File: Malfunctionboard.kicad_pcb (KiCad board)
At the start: 2 copper layers, 141.4 x 32.7 mm, 270 parts, among them J101 Conn_02x05_Odd_Even, J102 Conn_02x05_Odd_Even, J201 Conn_Coaxial, J202 Conn_Coaxial, J301 Conn_Coaxial, J302 Conn_Coaxial, J401 Conn_Coaxial, J402 Conn_Coaxial, J501 Conn_Coaxial, J502 Conn_Coaxial, J601 Conn_Coaxial, J602 Conn_Coaxial, J701 Conn_Coaxial, J702 Conn_Coaxial, J801 Conn_Coaxial, J802 Conn_Coaxial, J901 Conn_Coaxial, J902 Conn_Coaxial, Q101 NTR5103NT1G, Q102 RSC002P03T316, Q103 RSC002P03T316, Q104 NTR5103NT1G, Q201 NTR5103NT1G, Q202 NTR5103NT1G, Q301 NTR5103NT1G, Q302 NTR5103NT1G, Q401 NTR5103NT1G, Q402 NTR5103NT1G, Q501 NTR5103NT1G, Q502 NTR5103NT1G, Q601 NTR5103NT1G, Q602 NTR5103NT1G, Q701 NTR5103NT1G, Q702 NTR5103NT1G, Q801 NTR5103NT1G, Q802 NTR5103NT1G, Q901 NTR5103NT1G, Q902 NTR5103NT1G, U201 LM339PW, U301 LM339PW, U401 LM339PW, U501 LM339PW, U601 LM339PW, U701 LM339PW, U801 LM339PW, U901 LM339PW

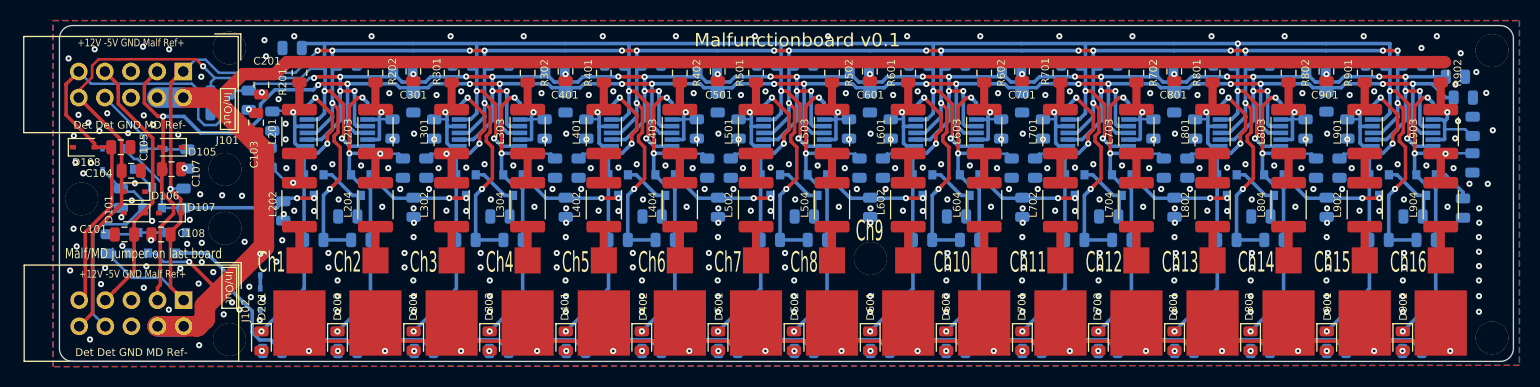
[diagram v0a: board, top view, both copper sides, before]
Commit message: Added: Through holes in the coaxial pads, for use as interfacebox module; README, LICENSE.
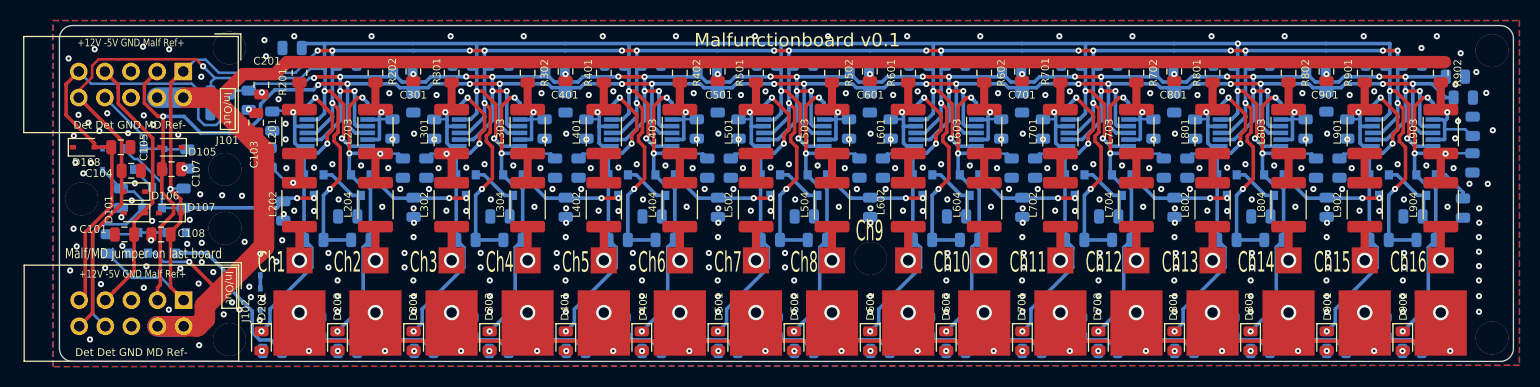
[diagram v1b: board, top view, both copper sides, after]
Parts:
- moved SYM101 3.86 mm to (110.2, 126.2)
- moved C812 1.02 mm to (183.3, 130.3)
- moved C212 1.02 mm to (94.5, 130.3)
- moved C312 1.02 mm to (109.3, 130.3)
- moved C412 1.02 mm to (124.1, 130.3)
- moved C512 1.02 mm to (138.9, 130.3)
- moved C612 1.02 mm to (153.7, 130.3)
- moved C712 1.02 mm to (168.5, 130.3)
- moved C912 1.02 mm to (198.1, 130.3)
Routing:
- net Net-(D701-Pad1): track 29.0 -> 29.6 mm
- net Net-(D501-Pad1): track 29.0 -> 29.6 mm
- net Net-(D801-Pad1): track 29.0 -> 29.6 mm
- net Net-(D301-Pad1): track 29.0 -> 29.6 mm
- net Net-(D601-Pad1): track 29.0 -> 29.6 mm
- net Net-(D901-Pad1): track 29.0 -> 29.6 mm
- net Net-(D401-Pad1): track 29.0 -> 29.6 mm
- net Net-(D201-Pad1): track 29.0 -> 29.5 mm
- net Net-(J902-Pad1): vias 0 -> 1
- net Net-(J901-Pad1): vias 0 -> 1
- net Net-(J802-Pad1): vias 0 -> 1
- net Net-(J801-Pad1): vias 0 -> 1
- net Net-(J702-Pad1): vias 0 -> 1
- net Net-(J701-Pad1): vias 0 -> 1
- net Net-(J602-Pad1): vias 0 -> 1
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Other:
- board text added: "(8ch:R101)"
- board text added: "02/2020 v0.1"
- board text removed: "11/2019 v0.1"

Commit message: Fixed: wrong pin layout for comparator
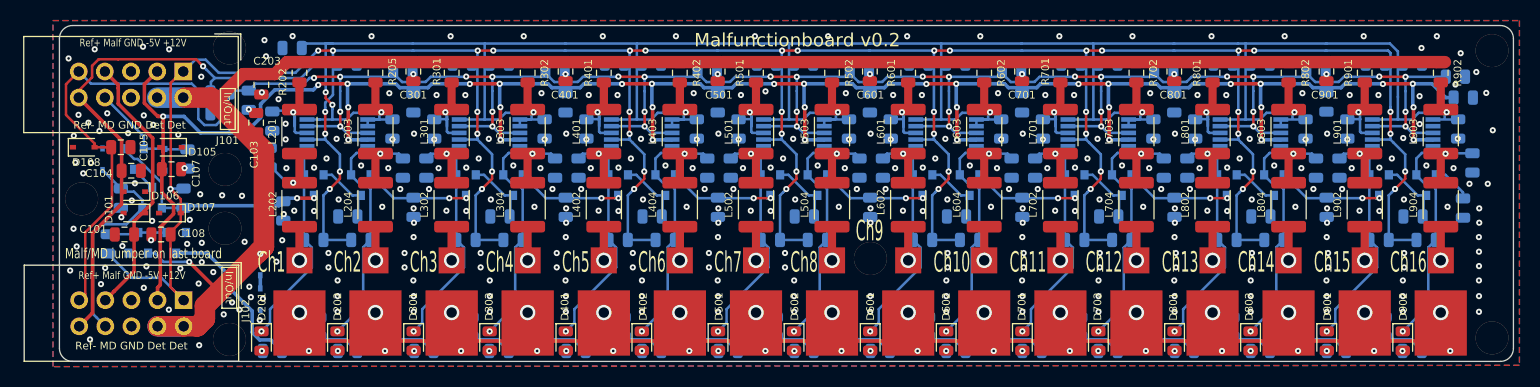
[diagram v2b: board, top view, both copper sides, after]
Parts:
- moved C904 1.44 mm to (205.2, 111.0), turned to 90 degrees
- renumbered C208 to C201, C209 to C202, C201 to C203, C210 to C204, C202 to C205, C203 to C206, C211 to C207, C206 to C208, C204 to C209, C207 to C210, C205 to C211, C309 to C307, C307 to C309, C409 to C407, C407 to C409, C509 to C507, C507 to C509, C609 to C607, C607 to C609, C709 to C707, C707 to C709, C809 to C807, C807 to C809, C909 to C907, C907 to C909, R203 to R201, R201 to R202, R204 to R203, R205 to R204, R202 to R205
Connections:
- C205 pad 2: Net-(C202-Pad2) -> Net-(C205-Pad2)
- C209 pad 2: Net-(C204-Pad2) -> Net-(C209-Pad2)
- C307 pad 2: +12V -> /Ref-
- C309 pad 2: /Ref- -> +12V
- C407 pad 2: +12V -> /Ref-
- C409 pad 2: /Ref- -> +12V
- C507 pad 2: +12V -> /Ref-
- C509 pad 2: /Ref- -> +12V
- C607 pad 2: +12V -> /Ref-
- C609 pad 2: /Ref- -> +12V
- C707 pad 2: +12V -> /Ref-
- C709 pad 2: /Ref- -> +12V
- C807 pad 2: +12V -> /Ref-
- C809 pad 2: /Ref- -> +12V
- C907 pad 2: +12V -> /Ref-
- C909 pad 2: /Ref- -> +12V
- L201 pad 2: Net-(C202-Pad2) -> Net-(C205-Pad2)
- L203 pad 2: Net-(C204-Pad2) -> Net-(C209-Pad2)
- R202 pad 2: Net-(C202-Pad2) -> Net-(C205-Pad2)
- R205 pad 2: Net-(C204-Pad2) -> Net-(C209-Pad2)
- U201 pad 10: /Ref+ -> Net-(C209-Pad2)
- U201 pad 11: -5V -> /Ref+
- U201 pad 12: Net-(C204-Pad2) -> -5V
- U201 pad 13: /Ref- -> Net-(D202-Pad1)
- U201 pad 2: Net-(C202-Pad2) -> Net-(D201-Pad1)
- U201 pad 3: /Ref+ -> +12V
- U201 pad 4: +12V -> Net-(C205-Pad2)
- U201 pad 5: Net-(C202-Pad2) -> /Ref+
- U201 pad 7: Net-(D201-Pad1) -> Net-(C205-Pad2)
- U201 pad 8: Net-(D202-Pad1) -> /Ref-
- U201 pad 9: Net-(C204-Pad2) -> Net-(C209-Pad2)
- U301 pad 10: /Ref+ -> Net-(C304-Pad2)
- U301 pad 11: -5V -> /Ref+
- U301 pad 12: Net-(C304-Pad2) -> -5V
- U301 pad 13: /Ref- -> Net-(D302-Pad1)
- U301 pad 2: Net-(C302-Pad2) -> Net-(D301-Pad1)
- U301 pad 3: /Ref+ -> +12V
- U301 pad 4: +12V -> Net-(C302-Pad2)
- U301 pad 5: Net-(C302-Pad2) -> /Ref+
- U301 pad 7: Net-(D301-Pad1) -> Net-(C302-Pad2)
- U301 pad 8: Net-(D302-Pad1) -> /Ref-
- U401 pad 10: /Ref+ -> Net-(C404-Pad2)
- U401 pad 11: -5V -> /Ref+
- U401 pad 12: Net-(C404-Pad2) -> -5V
- U401 pad 13: /Ref- -> Net-(D402-Pad1)
- U401 pad 2: Net-(C402-Pad2) -> Net-(D401-Pad1)
- U401 pad 3: /Ref+ -> +12V
- U401 pad 4: +12V -> Net-(C402-Pad2)
- U401 pad 5: Net-(C402-Pad2) -> /Ref+
- U401 pad 7: Net-(D401-Pad1) -> Net-(C402-Pad2)
- U401 pad 8: Net-(D402-Pad1) -> /Ref-
- U501 pad 10: /Ref+ -> Net-(C504-Pad2)
- U501 pad 11: -5V -> /Ref+
- U501 pad 12: Net-(C504-Pad2) -> -5V
- U501 pad 13: /Ref- -> Net-(D502-Pad1)
- U501 pad 2: Net-(C502-Pad2) -> Net-(D501-Pad1)
- U501 pad 3: /Ref+ -> +12V
- U501 pad 4: +12V -> Net-(C502-Pad2)
- U501 pad 5: Net-(C502-Pad2) -> /Ref+
- U501 pad 7: Net-(D501-Pad1) -> Net-(C502-Pad2)
- U501 pad 8: Net-(D502-Pad1) -> /Ref-
- U601 pad 10: /Ref+ -> Net-(C604-Pad2)
- U601 pad 11: -5V -> /Ref+
- U601 pad 12: Net-(C604-Pad2) -> -5V
- U601 pad 13: /Ref- -> Net-(D602-Pad1)
- U601 pad 2: Net-(C602-Pad2) -> Net-(D601-Pad1)
- U601 pad 3: /Ref+ -> +12V
- U601 pad 4: +12V -> Net-(C602-Pad2)
- U601 pad 5: Net-(C602-Pad2) -> /Ref+
- U601 pad 7: Net-(D601-Pad1) -> Net-(C602-Pad2)
- U601 pad 8: Net-(D602-Pad1) -> /Ref-
- U701 pad 10: /Ref+ -> Net-(C704-Pad2)
- U701 pad 11: -5V -> /Ref+
- U701 pad 12: Net-(C704-Pad2) -> -5V
- U701 pad 13: /Ref- -> Net-(D702-Pad1)
- U701 pad 2: Net-(C702-Pad2) -> Net-(D701-Pad1)
- U701 pad 3: /Ref+ -> +12V
- U701 pad 4: +12V -> Net-(C702-Pad2)
- U701 pad 5: Net-(C702-Pad2) -> /Ref+
- U701 pad 7: Net-(D701-Pad1) -> Net-(C702-Pad2)
- U701 pad 8: Net-(D702-Pad1) -> /Ref-
- U801 pad 10: /Ref+ -> Net-(C804-Pad2)
- U801 pad 11: -5V -> /Ref+
- U801 pad 12: Net-(C804-Pad2) -> -5V
- U801 pad 13: /Ref- -> Net-(D802-Pad1)
- U801 pad 2: Net-(C802-Pad2) -> Net-(D801-Pad1)
- U801 pad 3: /Ref+ -> +12V
- U801 pad 4: +12V -> Net-(C802-Pad2)
- U801 pad 5: Net-(C802-Pad2) -> /Ref+
- U801 pad 7: Net-(D801-Pad1) -> Net-(C802-Pad2)
- U801 pad 8: Net-(D802-Pad1) -> /Ref-
- U901 pad 10: /Ref+ -> Net-(C904-Pad2)
- U901 pad 11: -5V -> /Ref+
- U901 pad 12: Net-(C904-Pad2) -> -5V
- U901 pad 13: /Ref- -> Net-(D902-Pad1)
- U901 pad 2: Net-(C902-Pad2) -> Net-(D901-Pad1)
- U901 pad 3: /Ref+ -> +12V
- U901 pad 4: +12V -> Net-(C902-Pad2)
- U901 pad 5: Net-(C902-Pad2) -> /Ref+
- U901 pad 7: Net-(D901-Pad1) -> Net-(C902-Pad2)
- U901 pad 8: Net-(D902-Pad1) -> /Ref-
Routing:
- net /Ref-: track 305.4 -> 276.0 mm, vias 18 -> 3
- net /Ref+: track 284.1 -> 258.6 mm
- net +12V: track 375.5 -> 351.9 mm, vias 33 -> 47
- net Net-(C205-Pad2): track 0.00 -> 10.6 mm, vias 0 -> 1
- net Net-(C202-Pad2): track 10.5 -> 0.00 mm, vias 1 -> 0
- net Net-(C204-Pad2): track 8.92 -> 0.00 mm, vias 1 -> 0
- net Net-(D301-Pad1): track 29.6 -> 20.7 mm, vias 3 -> 1
- net Net-(D801-Pad1): track 29.6 -> 20.7 mm, vias 3 -> 1
- net Net-(D601-Pad1): track 29.6 -> 20.7 mm, vias 3 -> 1
- net Net-(D201-Pad1): track 29.5 -> 20.7 mm, vias 3 -> 1
- net Net-(D901-Pad1): track 29.6 -> 20.7 mm, vias 3 -> 1
- net Net-(D501-Pad1): track 29.6 -> 20.7 mm, vias 3 -> 1
- net Net-(D401-Pad1): track 29.6 -> 20.7 mm, vias 3 -> 1
- net Net-(D701-Pad1): track 29.6 -> 20.8 mm, vias 3 -> 1
- net -5V: track 214.6 -> 223.3 mm, vias 17 -> 33
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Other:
- board text added: "03/2020 v0.2"
- board text added: "Malfunctionboard v0.2"
- board text removed: "02/2020 v0.1"
- board text removed: "Malfunctionboard v0.1"

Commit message: Changed: Adjusted the in/out connectors for new driverboard (v0.3)
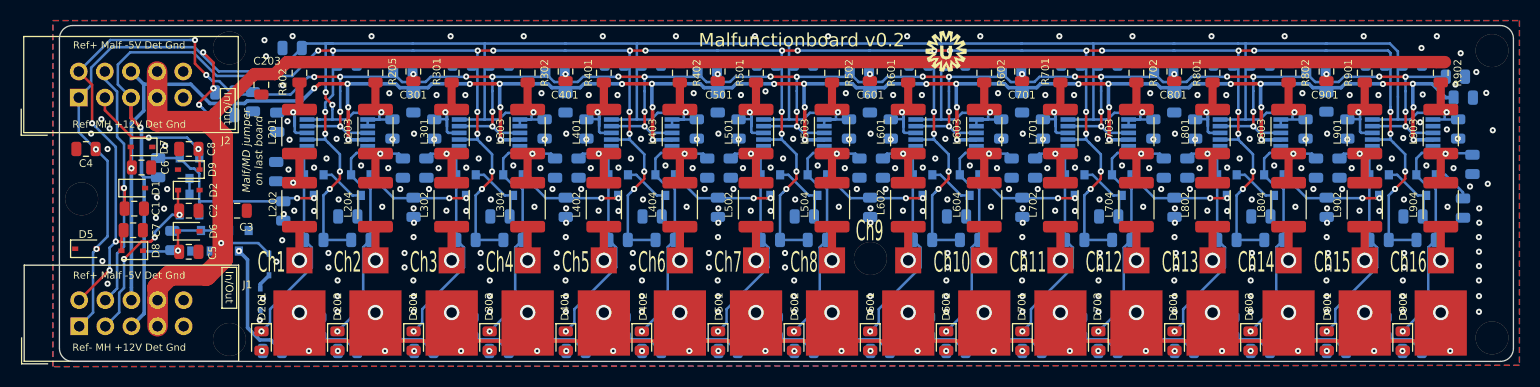
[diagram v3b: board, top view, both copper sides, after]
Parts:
- removed H101 (x2): MH_Pad, _Custom:MountingHole_3.2mm_M3_plated
- removed J101: Conn_02x05_Odd_Even, Connector_IDC:IDC-Header_2x05_P2.54mm_Vertical
- removed R104: R_Ref-, Resistor_SMD:R_0805_2012Metric
- removed R105: R_Ref, Resistor_SMD:R_0805_2012Metric
- removed R106: R_Ref+, Resistor_SMD:R_0805_2012Metric
- added G***: LOGO, _Custom:UMC_logo_4mm, F.Cu at (155.4, 103.4)
- added J2: In/out1, Connector_IDC:IDC-Header_2x05_P2.54mm_Vertical, F.Cu at (71.1, 108.0)
- added R1: R_Ref-, Resistor_SMD:R_0805_2012Metric, B.Cu at (85.3, 109.6)
- added R2: R_Ref, Resistor_SMD:R_0805_2012Metric, B.Cu at (85.3, 107.4)
- added R3: R_Ref+, Resistor_SMD:R_0805_2012Metric, B.Cu at (88.0, 108.3)
- C1: renamed from C101; value 10n -> 470pF
- C2: renamed from C102; value 10n -> 470pF; moved to F.Cu
- C203, C204, C205, C206, C207, C208, C209, C210, C211, C301, C302, C303, C304, C305, C306, C307, C310, C311, C401, C402, C403, C404, C405, C406, C407, C410, C411, C501, C502, C503, C504, C505, C506, C507, C510, C511, C601, C602, C603, C604, C605, C606, C607, C610, C611, C701, C702, C703, C704, C705, C706, C707, C710, C711, C801, C802, C803, C804, C805, C806, C807, C810, C811, C901, C902, C903, C904, C905, C906, C907, C910, C911: value 10n -> 470pF
- C3: renamed from C103; value 10n -> 470pF
- C4: renamed from C104; value 10n -> 470pF
- C7: renamed from C105; value 10n -> 470pF
- C8: renamed from C106; value 10n -> 470pF; moved to F.Cu
- D2: renamed from D102; moved to F.Cu
- D9: renamed from D109; moved to F.Cu
- J1: renamed from J102; value Conn_02x05_Odd_Even -> In/out1
- R6: renamed from R103; value 100k -> 10k
- moved D8 11.1 mm to (76.3, 122.8), turned to 180 degrees
- moved J1 10.5 mm to (71.1, 130.2), turned to 90 degrees
- moved C3 8.75 mm to (86.5, 118.9), turned to 180 degrees
- moved D9 8.45 mm to (81.8, 114.9), turned to 180 degrees
- moved C7 8.16 mm to (76.4, 120.8)
- moved C8 8.16 mm to (81.8, 112.9), turned to 0 degrees
- moved D5 7.28 mm to (71.8, 122.6), turned to 0 degrees
- moved Q2 6.98 mm to (81.9, 118.3), turned to 90 degrees
- moved R6 6.29 mm to (80.2, 121.8)
- moved Q4 6.10 mm to (86.7, 121.9)
- moved Q1 6.10 mm to (83.0, 121.9)
- moved C2 5.03 mm to (81.8, 118.9), turned to 180 degrees
- moved C4 4.89 mm to (71.8, 112.9), turned to 0 degrees
- moved Q3 4.63 mm to (81.9, 114.8), turned to 270 degrees
- moved R5 3.86 mm to (78.8, 114.8), turned to 90 degrees
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- renumbered C108 to C5, C107 to C6, D101 to D1, D103 to D3, D104 to D4, D106 to D5, D107 to D6, D105 to D7, D108 to D8, H102 to H1, H104 to H3, H105 to H4, H107 to H5, H108 to H6, H106 to H7, Q101 to Q1, Q102 to Q2, Q103 to Q3, Q104 to Q4, R101 to R4, R102 to R5, SYM101 to SYM1
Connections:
- C2 pad 2: Net-(C102-Pad2) -> /MH_1
- C203 pad 2: /V_in -> /V_detune
- C3 pad 2: /V_in -> /V_detune
- C301 pad 2: /V_in -> /V_detune
- C401 pad 2: /V_in -> /V_detune
- C501 pad 2: /V_in -> /V_detune
- C601 pad 2: /V_in -> /V_detune
- C701 pad 2: /V_in -> /V_detune
- C8 pad 2: Net-(C106-Pad2) -> /MH_2
- C801 pad 2: /V_in -> /V_detune
- C901 pad 2: /V_in -> /V_detune
- D2 pad 1: Net-(C102-Pad2) -> /MH_1
- D3 pad 2: /V_in -> /V_detune
- D9 pad 1: Net-(C106-Pad2) -> /MH_2
- J1 pad 1: +12V -> /Ref-
- J1 pad 10: /Ref- -> GND
- J1 pad 2: /V_in -> /Ref+
- J1 pad 3: -5V -> /MH_1
- J1 pad 4: /V_in -> /Malf
- J1 pad 5: GND -> +12V
- J1 pad 6: GND -> -5V
- J1 pad 7: /Malf -> /V_detune
- J1 pad 8: Net-(C106-Pad2) -> /V_detune
- J1 pad 9: /Ref+ -> GND
- Q1 pad 1: /V_in -> /V_detune
- Q2 pad 2: Net-(C102-Pad2) -> /MH_1
- Q3 pad 2: Net-(C106-Pad2) -> /MH_2
- R202 pad 1: /V_in -> /V_detune
- R205 pad 1: /V_in -> /V_detune
- R301 pad 1: /V_in -> /V_detune
- R302 pad 1: /V_in -> /V_detune
- R401 pad 1: /V_in -> /V_detune
- R402 pad 1: /V_in -> /V_detune
- R501 pad 1: /V_in -> /V_detune
- R502 pad 1: /V_in -> /V_detune
- R601 pad 1: /V_in -> /V_detune
- R602 pad 1: /V_in -> /V_detune
- R701 pad 1: /V_in -> /V_detune
- R702 pad 1: /V_in -> /V_detune
- R801 pad 1: /V_in -> /V_detune
- R802 pad 1: /V_in -> /V_detune
- R901 pad 1: /V_in -> /V_detune
- R902 pad 1: /V_in -> /V_detune
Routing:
- net /V_in: track 170.7 -> 0.00 mm, vias 2 -> 0
- net /V_detune: track 0.00 -> 163.7 mm, vias 0 -> 1
- net Net-(C106-Pad2): track 21.2 -> 0.00 mm
- net /MH_1: track 0.00 -> 16.8 mm, vias 0 -> 3
- net /MH_2: track 0.00 -> 14.8 mm, vias 0 -> 2
- net Net-(C102-Pad2): track 11.7 -> 0.00 mm
- net +12V: track 351.9 -> 357.2 mm, vias 47 -> 48
- net /sheet5DD8DCB3/LED_GND: track 141.1 -> 137.0 mm, vias 0 -> 1
- net /sheet5DD8DCB3/Malf_in: track 22.7 -> 20.1 mm
- net /Ref-: track 276.0 -> 278.4 mm, vias 3 -> 7
- net -5V: track 223.3 -> 221.3 mm
- net Net-(C206-Pad2): track 6.22 -> 4.88 mm
- net Net-(Q2-Pad3): track 2.42 -> 1.53 mm
- net /Malf: track 26.5 -> 25.8 mm, vias 0 -> 1
- net /Ref+: track 258.6 -> 258.0 mm, vias 32 -> 37
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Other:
- board text added: "Gnd Det +12V MH Ref-"
- board text added: "Gnd Det -5V Malf Ref+"
- board text added: "Ref+ Malf -5V Det Gnd"
- board text added: "Ref- MH +12V Det Gnd"
- board text removed: "+12V -5V GND Malf Ref+"
- board text removed: "Det Det GND MD Ref-"
- board text removed: "Ref+ Malf GND -5V +12V"
- board text removed: "Ref- MD GND Det Det"

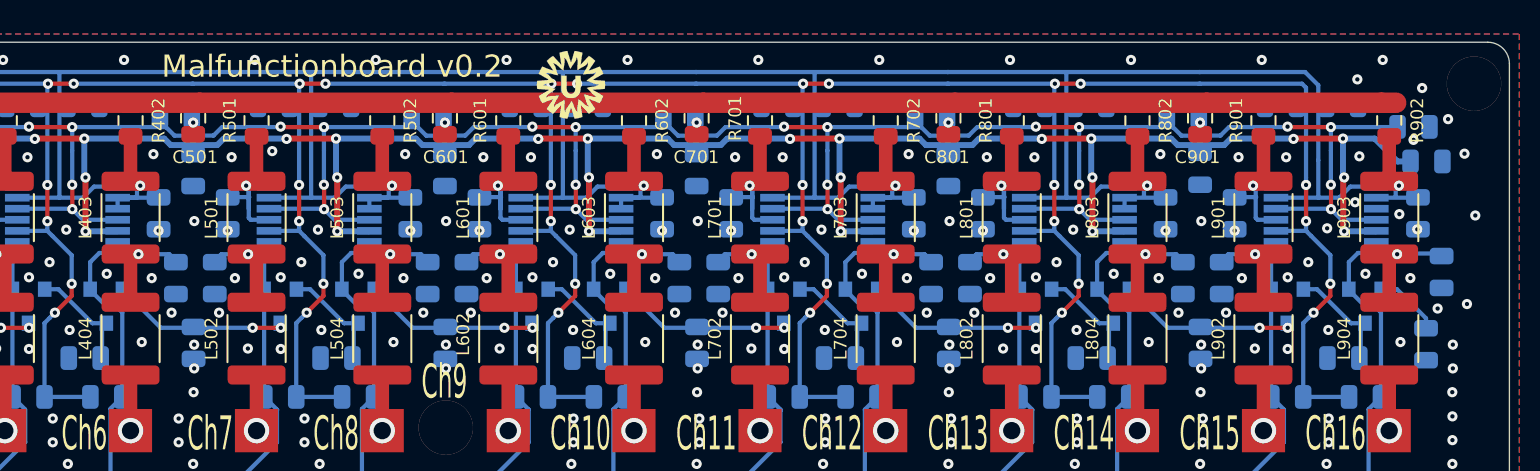
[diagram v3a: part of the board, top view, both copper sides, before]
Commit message: Changed: version number. Added: one missing track on comparator. Removed: resistor on internal malfunction
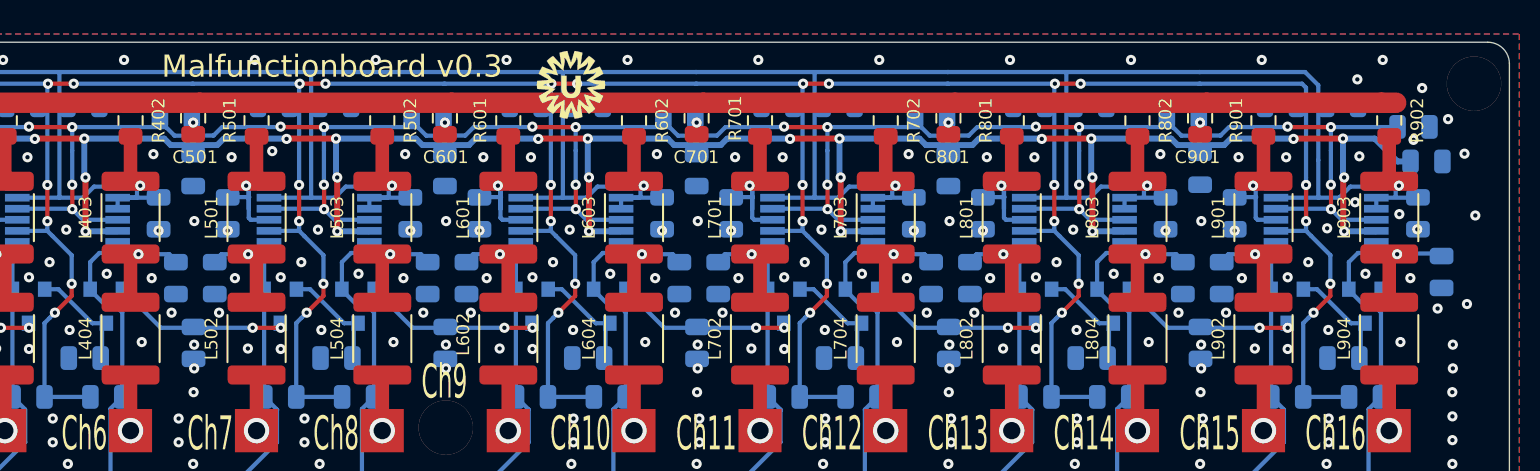
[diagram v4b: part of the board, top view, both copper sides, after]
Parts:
- removed R4: 10k, Resistor_SMD:R_0805_2012Metric
- D3: value 5V -> 5.4V
- J1, J2: value In/out1 -> In/out
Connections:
- Q902 pad 2: /sheet5DF3552C/Malf -> GND
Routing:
- net /sheet5DF3552C/Malf: track 3.95 -> 0.00 mm
- net Net-(C904-Pad2): track 5.75 -> 6.40 mm
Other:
- board text added: "04/2020 v0.3"
- board text added: "Malfunctionboard v0.3"
- board text removed: "03/2020 v0.2"
- board text removed: "Malfunctionboard v0.2"

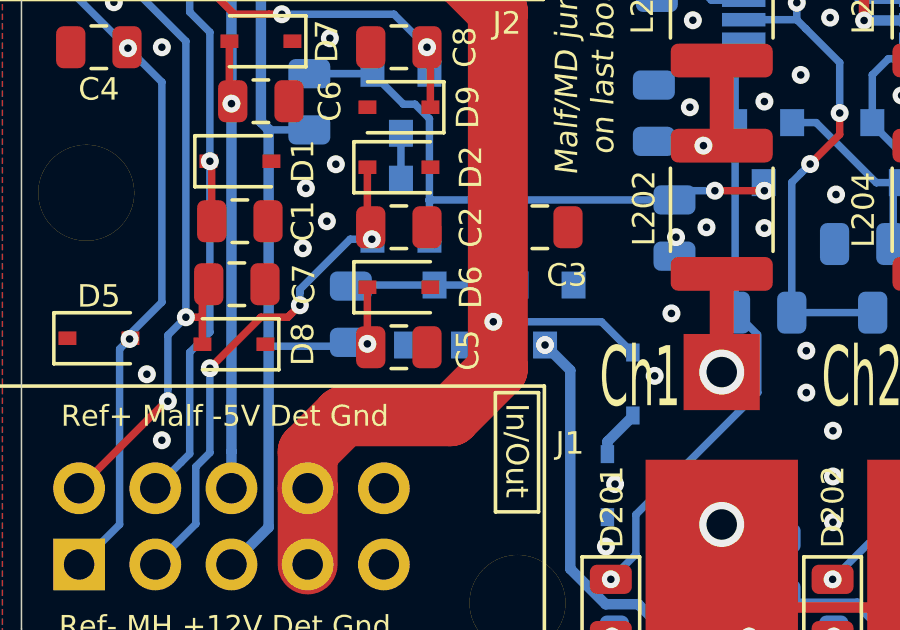
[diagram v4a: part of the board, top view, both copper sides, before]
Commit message: Changed: fixed mistake in turning off LED's during +12v on detune.
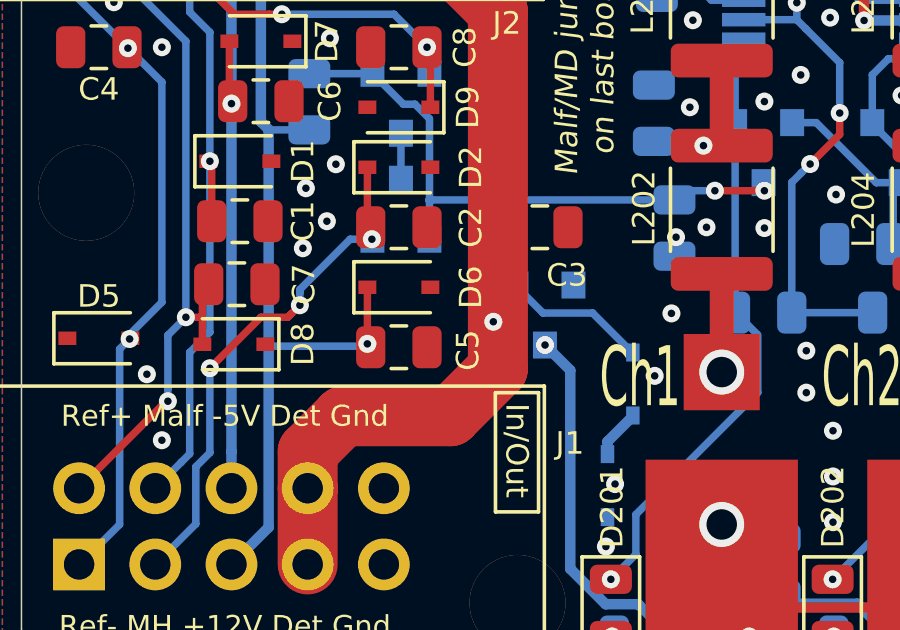
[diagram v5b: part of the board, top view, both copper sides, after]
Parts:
- removed Q4: NTR5103NT1G, Package_TO_SOT_SMD:SOT-23
- removed R6: 10k, Resistor_SMD:R_0805_2012Metric
- Q1: value NTR5103NT1G -> RSC002P03T316
- R5: value 10k -> 1k
- moved Q1 3.68 mm to (86.7, 121.9), turned to 270 degrees
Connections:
- Q1 pad 3: Net-(Q1-Pad3) -> /sheet5DD8DCB3/LED_GND
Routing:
- net Net-(Q1-Pad3): track 5.54 -> 0.00 mm
- net +12V: track 357.2 -> 357.9 mm

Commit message: Changed: resistor and zener diode values.
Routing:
- net GND: vias 324 -> 341
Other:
- board text added: "(8ch:0R)"
- board text removed: "(8ch:R101)"
- board text removed: "DW"
